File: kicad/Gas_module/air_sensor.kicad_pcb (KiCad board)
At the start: 2 copper layers, 95 x 75 mm, 28 parts, among them J1 Program Header, M1 MiCS-6814, U9 Buffer

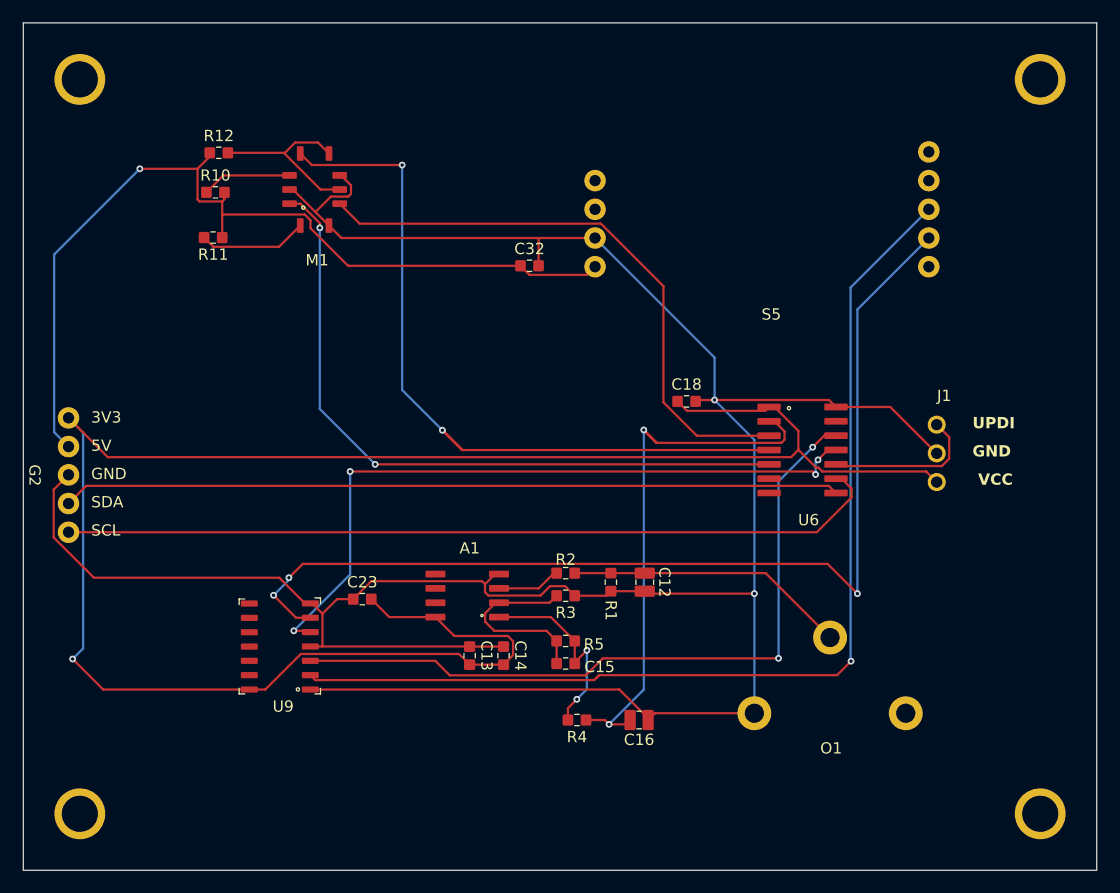
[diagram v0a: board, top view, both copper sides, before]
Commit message: added status LED to gas module
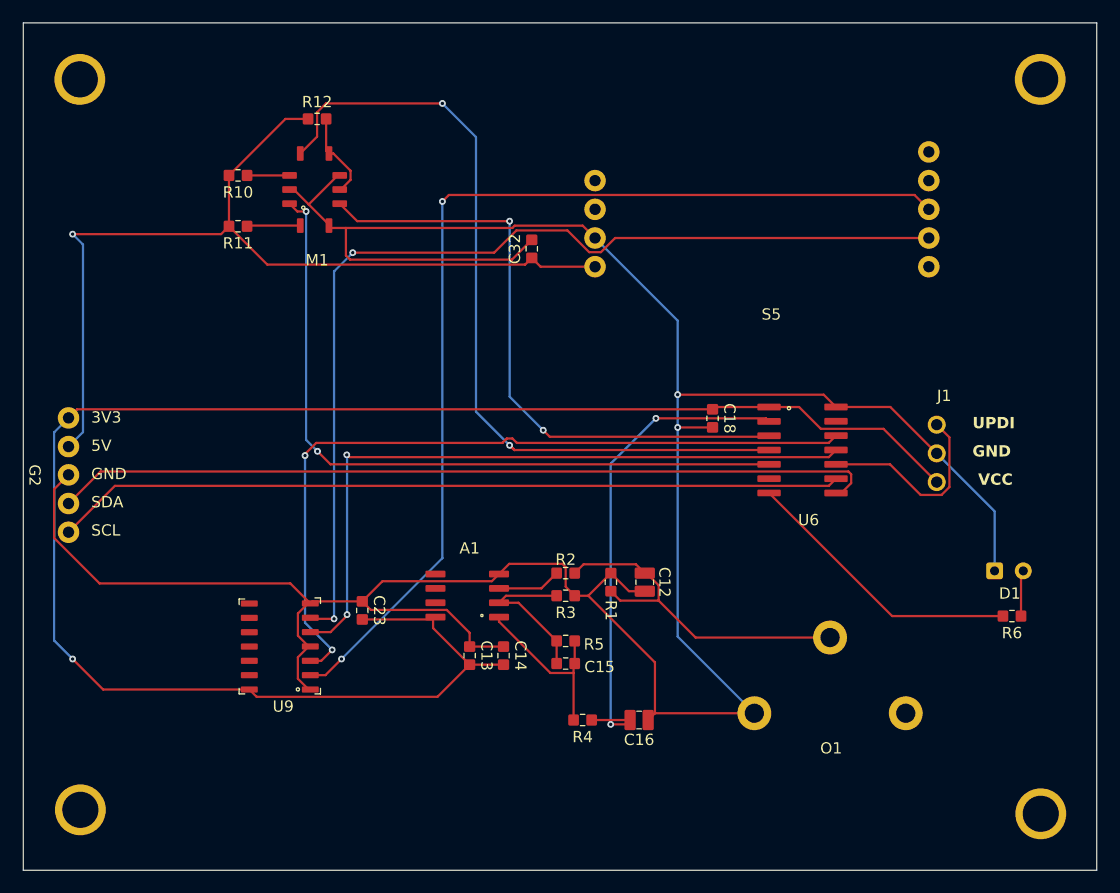
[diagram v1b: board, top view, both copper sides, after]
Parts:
- removed ? (x3): , 
- removed the REF** at (96.9, 72.7)
- added D1: ~, common:LED_3mm_THT, F.Cu at (179.3, 109.5)
- added R6: 220, common:R_0603, F.Cu at (179.5, 110.5)
- added REF**: mounting_hole, air_sens_foots:mounting_hole, F.Cu at (176.9, 67.7)
- added REF**: mounting_hole, air_sens_foots:mounting_hole, F.Cu at (176.9, 132.7)
- added REF**: mounting_hole, air_sens_foots:mounting_hole, F.Cu at (92.0, 132.3)
- added REF**: mounting_hole, air_sens_foots:mounting_hole, F.Cu at (91.9, 67.7)
- moved R12 9.20 mm to (118.0, 66.5)
- moved C18 2.75 mm to (153.0, 93.0), turned to -90 degrees
- moved R10 2.50 mm to (111.0, 71.5), turned to 180 degrees
- moved R11 2.42 mm to (111.0, 76.0), turned to 180 degrees
- moved C32 1.51 mm to (137.0, 78.0), turned to 90 degrees
- moved C23 1.00 mm to (122.0, 110.0), turned to -90 degrees
- moved R4 0.50 mm to (141.5, 119.7)
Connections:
- O1 pad 3: (no net) -> unconnected-(O1-Pad3)
- R1 pad 1: Net-(O1-Vsensor+) -> GND
- R1 pad 2: GND -> Net-(O1-Vsensor+)
- U6 pad 7: unconnected-(U6-TOSC2/PB2-Pad7) -> STATUS_LED
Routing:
- net STATUS_LED: track 0.00 -> 25.2 mm
- net 3V3: track 173.2 -> 155.1 mm
- net GND: track 244.7 -> 254.1 mm
- net Net-(M1-E): track 16.0 -> 7.83 mm
- net 02_A: track 50.3 -> 44.1 mm
- net Net-(O1-Vsensor+): track 25.0 -> 31.0 mm
- net Net-(M1-K): track 9.63 -> 4.73 mm
- net Net-(M1-C): track 7.98 -> 3.76 mm
- net SDA: track 68.8 -> 73.0 mm
- net Net-(D1-A): track 0.00 -> 4.08 mm
- net AT_GAS_RX: track 65.2 -> 69.2 mm
- net C02_RX: track 92.2 -> 88.3 mm, vias 3 -> 2
- net NH3_VAL: track 69.0 -> 72.7 mm
- net UPDI: track 13.8 -> 17.4 mm
- net SCL: track 73.1 -> 69.9 mm
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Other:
- board text added: "${REFERENCE}"

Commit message: added 1206 smd capacitor footprint
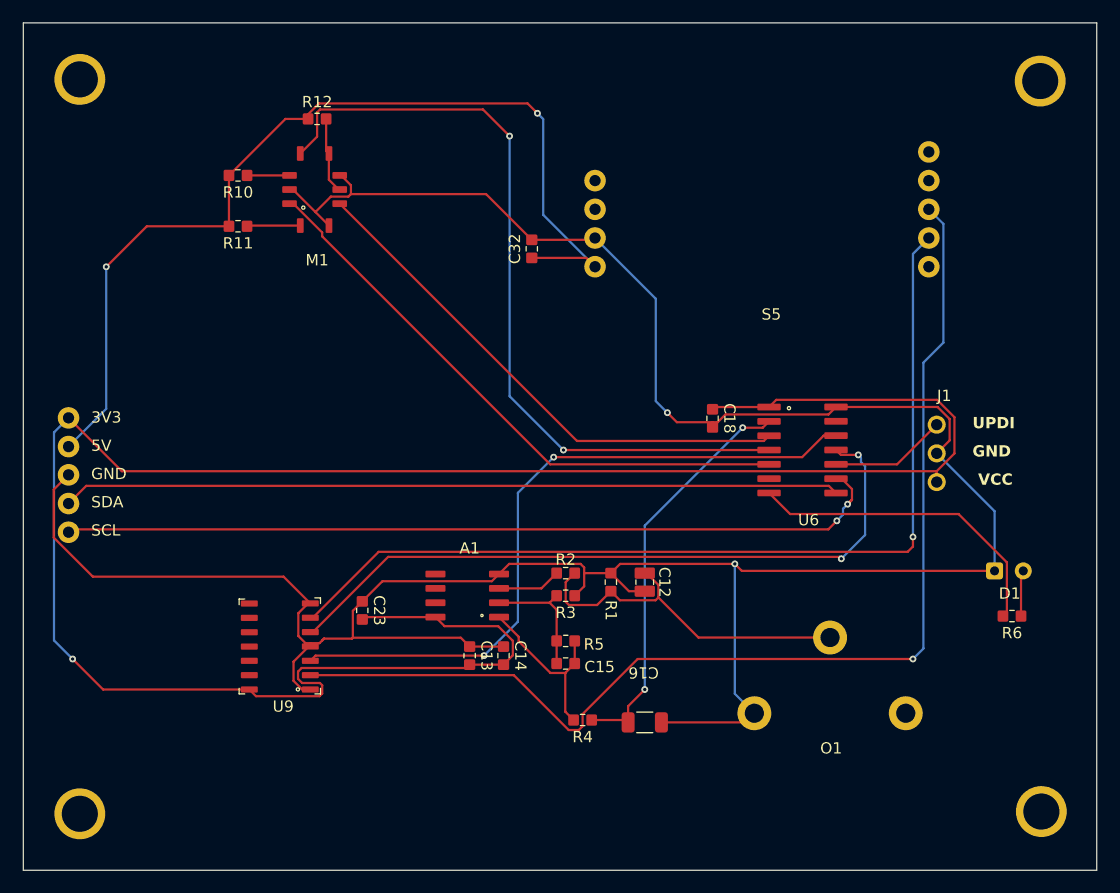
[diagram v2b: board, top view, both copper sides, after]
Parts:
- removed the REF** at (176.9, 67.7)
- removed the REF** at (176.9, 132.7)
- removed the REF** at (92.0, 132.3)
- removed the REF** at (91.9, 67.7)
- added REF**: mounting_hole, air_sens_foots:mounting_hole, F.Cu at (96.9, 72.7)
- added REF**: mounting_hole, air_sens_foots:mounting_hole, F.Cu at (181.9, 72.8)
- added REF**: mounting_hole, air_sens_foots:mounting_hole, F.Cu at (96.9, 137.7)
- added REF**: mounting_hole, air_sens_foots:mounting_hole, F.Cu at (182.0, 137.5)
- C16: footprint common:C_0805 -> common:C_1206
- moved C16 0.50 mm to (147.0, 119.7)
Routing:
- net 3V3: track 155.1 -> 192.6 mm
- net NO2_VAL: track 63.8 -> 52.2 mm, vias 2 -> 0
- net GND: track 254.1 -> 245.3 mm
- net CO_VAL: track 55.7 -> 46.9 mm, vias 2 -> 0
- net CO2_TX: track 91.4 -> 100.0 mm, vias 2 -> 1
- net 02_A: track 44.1 -> 36.2 mm
- net AT_GAS_RX: track 69.2 -> 61.5 mm
- net UPDI: track 17.4 -> 10.4 mm
- net SCL: track 69.9 -> 74.7 mm, vias 0 -> 2
- net C02_RX: track 88.3 -> 83.8 mm, vias 2 -> 1
- net 5V: track 81.8 -> 86.3 mm, vias 1 -> 2
- net SDA: track 73.0 -> 68.8 mm
- net STATUS_LED: track 25.2 -> 28.5 mm
- net Net-(A1--IN_A): track 13.9 -> 11.0 mm
- net NH3_VAL: track 72.7 -> 70.3 mm
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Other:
- board text removed: "${REFERENCE}"
